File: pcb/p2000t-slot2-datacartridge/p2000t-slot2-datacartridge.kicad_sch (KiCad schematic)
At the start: 27 parts, among them J1 P2000T Port 2, U1 74HC02, U10 ZIF, U11 CY62256-70PC, U2 74HC04, U3 74HC138, U4 74HC21, U5 74HC273, U6 74HC273, U7 74HC173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

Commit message: Initial commit revision
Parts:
- added unit 6 of U2
- U11: footprint Package_DIP:DIP-28_W15.24mm_Socket -> Package_DIP:DIP-28_W15.24mm
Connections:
- net GND: now also U2.13
- net A3: now reaches J1.7b (Pin_7b)
- net A3: now also U2.5
- net M1: no longer names the net of J1.11b (Pin_11b)
- net M1: no longer U2.5
- no-connect marks 11 -> 12
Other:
- note added: "M1"
- moved on the sheet: U4B

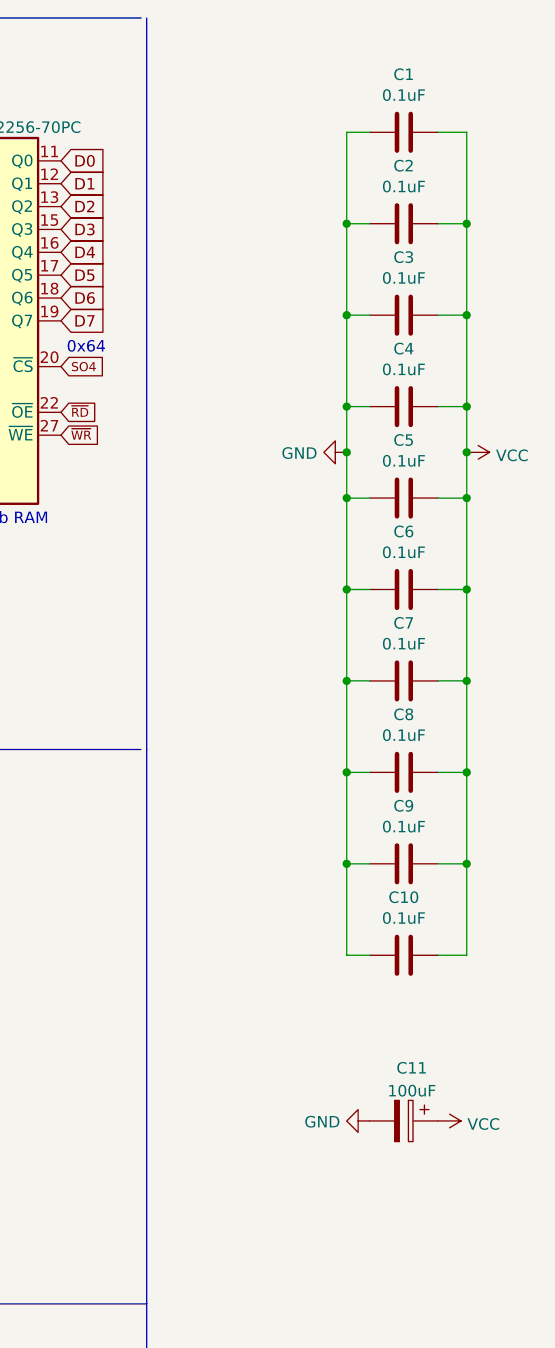
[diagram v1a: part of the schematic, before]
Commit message: Rerouting
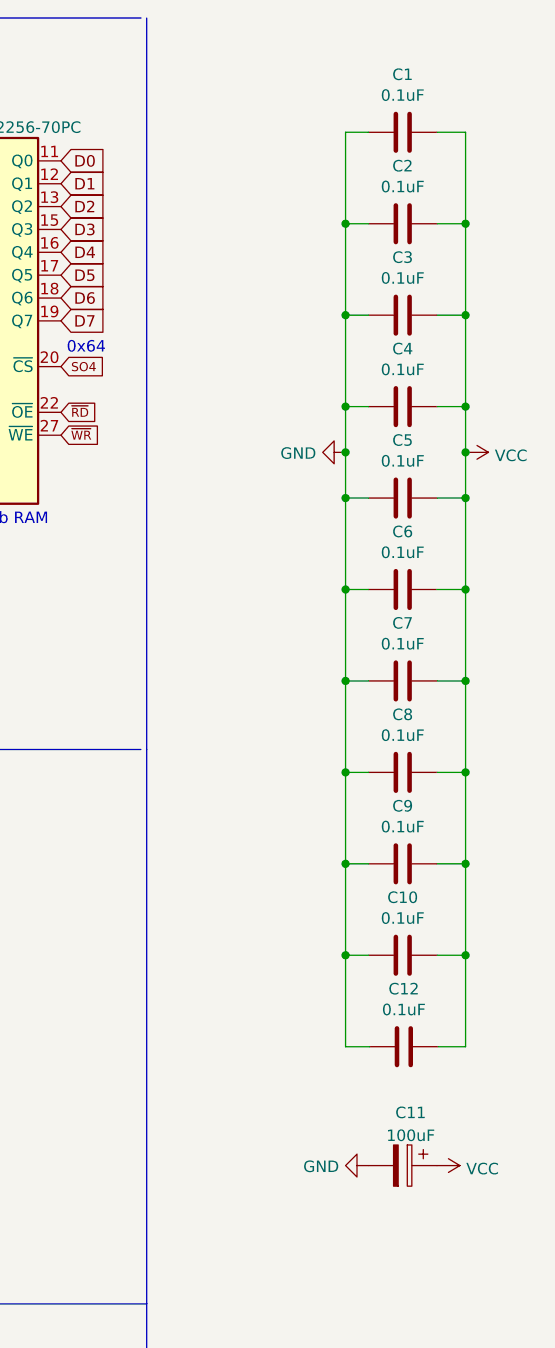
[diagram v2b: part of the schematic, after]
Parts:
- added C12: 0.1uF, Capacitor_THT:C_Disc_D5.0mm_W2.5mm_P5.00mm, symbol Device:C
- U11: footprint Package_DIP:DIP-28_W15.24mm -> Package_DIP:DIP-28_W15.24mm_Socket
- U2: footprint (none) -> Package_DIP:DIP-14_W7.62mm_Socket
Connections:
- net GND: now also C12.2
- net VCC: now also C12.1
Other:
- moved on the sheet: C11

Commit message: Fixing bug in PCB
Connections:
- net A3: now also U3.4 (E1); no longer U2.5
- net GND: now also U2.5
- net at U2.6: no longer U3.4 (E1)
- no-connect marks 12 -> 13
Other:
- moved on the sheet: U2C, U2F, U4B
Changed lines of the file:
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@@
   (junction (at 253.365 125.095) (diameter 0) (color 0 0 0 0)
   )
-  (junction (at 87.63 177.8) (diameter 0) (color 0 0 0 0)
+  (junction (at 85.979 179.451) (diameter 0) (color 0 0 0 0)
   )
   (junction (at 170.815 84.455) (diameter 0) (color 0 0 0 0)
@@
   (junction (at 253.365 131.445) (diameter 0) (color 0 0 0 0)
   )
-  (junction (at 87.63 180.34) (diameter 0) (color 0 0 0 0)
+  (junction (at 85.979 181.991) (diameter 0) (color 0 0 0 0)
   )
   (junction (at 373.888 78.74) (diameter 0) (color 0 0 0 0)
@@
   (junction (at 373.888 63.5) (diameter 0) (color 0 0 0 0)
   )
-  (junction (at 87.63 182.88) (diameter 0) (color 0 0 0 0)
+  (junction (at 85.979 184.531) (diameter 0) (color 0 0 0 0)
   )
   (no_connect (at 54.61 189.23))
-  (no_connect (at 102.87 179.07))
+  (no_connect (at 101.219 180.721))
   (no_connect (at 49.53 176.53))
   (no_connect (at 57.15 189.23))
   (no_connect (at 52.07 189.23))
-  (no_connect (at 108.585 194.945))
+  (no_connect (at 106.934 196.596))
   (no_connect (at 196.215 71.755))
   (no_connect (at 280.67 118.745))
   (no_connect (at 62.865 61.595))
   (no_connect (at 280.67 116.205))
+  (no_connect (at 114.3 167.513))
   (no_connect (at 24.13 189.23))
   (no_connect (at 54.61 176.53))
@@
     (stroke (width 0) (type default))
   )
-  (wire (pts (xy 87.63 177.8) (xy 87.63 180.34))
+  (wire (pts (xy 85.979 179.451) (xy 85.979 181.991))
     (stroke (width 0) (type default))
   )
@@
     (stroke (width 0) (type default))
   )
-  (wire (pts (xy 87.63 175.26) (xy 87.63 177.8))
+  (wire (pts (xy 85.979 176.911) (xy 85.979 179.451))
     (stroke (width 0) (type default))
   )
@@
     (stroke (width 0) (type default))
   )
-  (wire (pts (xy 62.865 93.98) (xy 62.865 86.995))
-    (stroke (width 0) (type default))
-  )
   (wire (pts (xy 268.605 76.835) (xy 271.78 76.835))
     (stroke (width 0) (type default))
@@
     (stroke (width 0) (type default))
   )
-  (wire (pts (xy 87.63 180.34) (xy 87.63 182.88))
+  (wire (pts (xy 85.979 181.991) (xy 85.979 184.531))
     (stroke (width 0) (type default))
   )
@@
     (stroke (width 0) (type default))
   )
-  (wire (pts (xy 87.63 182.88) (xy 87.63 184.785))
+  (wire (pts (xy 85.979 184.531) (xy 85.979 186.436))
     (stroke (width 0) (type default))
   )
@@
     )
   )
-  (global_label "A3" (shape input) (at 62.865 109.22 270) (fields_autoplaced)
+  (global_label "A3" (shape input) (at 62.865 86.995 270) (fields_autoplaced)
     (effects (font (size 1.27 1.27)) (justify right))
-    (property "Intersheetrefs" "${INTERSHEET_REFS}" (at 62.865 113.8491 90)
+    (property "Intersheetrefs" "${INTERSHEET_REFS}" (at 62.865 91.6241 90)
       (effects (font (size 1.27 1.27)) (justify right) hide)
     )
@@
     )
   )
-  (symbol (lib_id "74xx:74LS21") (at 95.25 179.07 0) (unit 2)
+  (symbol (lib_id "74xx:74LS21") (at 93.599 180.721 0) (unit 2)
     (in_bom yes) (on_board yes) (dnp no)
-    (property "Reference" "U4" (at 95.25 169.545 0)
+    (property "Reference" "U4" (at 93.599 171.196 0)
       (effects (font (size 1.27 1.27)))
     )
-    (property "Value" "74HC21" (at 95.25 171.8564 0)
+    (property "Value" "74HC21" (at 93.599 173.5074 0)
       (effects (font (size 1.27 1.27)))
     )
-    (property "Footprint" "Package_DIP:DIP-14_W7.62mm_Socket" (at 95.25 179.07 0)
+    (property "Footprint" "Package_DIP:DIP-14_W7.62mm_Socket" (at 93.599 180.721 0)
       (effects (font (size 1.27 1.27)) hide)
     )
-    (property "Datasheet" "http://www.ti.com/lit/gpn/sn74LS21" (at 95.25 179.07 0)
+    (property "Datasheet" "http://www.ti.com/lit/gpn/sn74LS21" (at 93.599 180.721 0)
       (effects (font (size 1.27 1.27)) hide)
     )
@@
     )
   )
-  (symbol (lib_id "74xx:74HC04") (at 62.865 101.6 90) (unit 3)
+  (symbol (lib_id "74xx:74HC04") (at 106.68 167.513 0) (unit 3)
     (in_bom yes) (on_board yes) (dnp no)
-    (property "Reference" "U2" (at 67.437 100.4316 90)
+    (property "Reference" "U2" (at 110.871 162.56 0)
       (effects (font (size 1.27 1.27)) (justify right))
     )
-    (property "Value" "74HC04" (at 67.437 102.743 90)
+    (property "Value" "74HC04" (at 112.776 164.592 0)
       (effects (font (size 1.27 1.27)) (justify right))
     )
-    (property "Footprint" "Package_DIP:DIP-14_W7.62mm_Socket" (at 62.865 101.6 0)
+    (property "Footprint" "Package_DIP:DIP-14_W7.62mm_Socket" (at 106.68 167.513 0)
       (effects (font (size 1.27 1.27)) hide)
     )
-    (property "Datasheet" "https://assets.nexperia.com/documents/data-sheet/74HC_HCT04.pdf" (at 62.865 101.6 0)
+    (property "Datasheet" "https://assets.nexperia.com/documents/data-sheet/74HC_HCT04.pdf" (at 106.68 167.513 0)
       (effects (font (size 1.27 1.27)) hide)
     )
@@
     )
   )
-  (symbol (lib_id "power:GND") (at 87.63 184.785 0) (unit 1)
+  (symbol (lib_id "power:GND") (at 99.06 167.513 270) (unit 1)
+    (in_bom yes) (on_board yes) (dnp no)
+    (property "Reference" "#PWR040" (at 92.71 167.513 0)
+      (effects (font (size 1.27 1.27)) hide)
+    )
+    (property "Value" "GND" (at 95.8088 167.64 90)
+      (effects (font (size 1.27 1.27)) (justify right))
+    )
+    (property "Footprint" "" (at 99.06 167.513 0)
+      (effects (font (size 1.27 1.27)) hide)
+    )
+    (property "Datasheet" "" (at 99.06 167.513 0)
+      (effects (font (size 1.27 1.27)) hide)
+    )
+    (pin "1")
+    (instances
+      (project "p2000t-slot2-datacartridge"
+        (path "/4756119e-5b4c-4d38-8569-93d77ea2213d"
+          (reference "#PWR040") (unit 1)
+        )
+      )
+    )
+  )
+  (symbol (lib_id "power:GND") (at 85.979 186.436 0) (unit 1)
     (in_bom yes) (on_board yes) (dnp no)
-    (property "Reference" "#PWR017" (at 87.63 191.135 0)
+    (property "Reference" "#PWR017" (at 85.979 192.786 0)
       (effects (font (size 1.27 1.27)) hide)
     )
-    (property "Value" "GND" (at 87.757 188.0362 90)
+    (property "Value" "GND" (at 86.106 189.6872 90)
       (effects (font (size 1.27 1.27)) (justify right))
     )
-    (property "Footprint" "" (at 87.63 184.785 0)
+    (property "Footprint" "" (at 85.979 186.436 0)
       (effects (font (size 1.27 1.27)) hide)
     )
-    (property "Datasheet" "" (at 87.63 184.785 0)
+    (property "Datasheet" "" (at 85.979 186.436 0)
       (effects (font (size 1.27 1.27)) hide)
     )
@@
     )
   )
-  (symbol (lib_id "74xx:74HC04") (at 100.965 194.945 0) (unit 6)
+  (symbol (lib_id "74xx:74HC04") (at 99.314 196.596 0) (unit 6)
     (in_bom yes) (on_board yes) (dnp no)
-    (property "Reference" "U2" (at 100.965 186.69 0)
+    (property "Reference" "U2" (at 99.314 188.341 0)
       (effects (font (size 1.27 1.27)))
     )
-    (property "Value" "74HC04" (at 100.965 189.23 0)
+    (property "Value" "74HC04" (at 99.314 190.881 0)
       (effects (font (size 1.27 1.27)))
     )
-    (property "Footprint" "Package_DIP:DIP-14_W7.62mm_Socket" (at 100.965 194.945 0)
+    (property "Footprint" "Package_DIP:DIP-14_W7.62mm_Socket" (at 99.314 196.596 0)
       (effects (font (size 1.27 1.27)) hide)
     )
-    (property "Datasheet" "https://assets.nexperia.com/documents/data-sheet/74HC_HCT04.pdf" (at 100.965 194.945 0)
+    (property "Datasheet" "https://assets.nexperia.com/documents/data-sheet/74HC_HCT04.pdf" (at 99.314 196.596 0)
       (effects (font (size 1.27 1.27)) hide)
     )
@@
     )
   )
-  (symbol (lib_id "power:GND") (at 93.345 194.945 270) (unit 1)
+  (symbol (lib_id "power:GND") (at 91.694 196.596 270) (unit 1)
     (in_bom yes) (on_board yes) (dnp no)
-    (property "Reference" "#PWR020" (at 86.995 194.945 0)
+    (property "Reference" "#PWR020" (at 85.344 196.596 0)
       (effects (font (size 1.27 1.27)) hide)
     )
-    (property "Value" "GND" (at 90.0938 195.072 90)
+    (property "Value" "GND" (at 88.4428 196.723 90)
       (effects (font (size 1.27 1.27)) (justify right))
     )
-    (property "Footprint" "" (at 93.345 194.945 0)
+    (property "Footprint" "" (at 91.694 196.596 0)
       (effects (font (size 1.27 1.27)) hide)
     )
-    (property "Datasheet" "" (at 93.345 194.945 0)
+    (property "Datasheet" "" (at 91.694 196.596 0)
       (effects (font (size 1.27 1.27)) hide)
     )
